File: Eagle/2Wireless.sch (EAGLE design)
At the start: 17 parts, among them IC1 TCA9517A, IC2 VREGLD1117, IC3 MB85RS2MTAPNF-G-BDERE1, U1 PHOTON_WITH_HEADERS

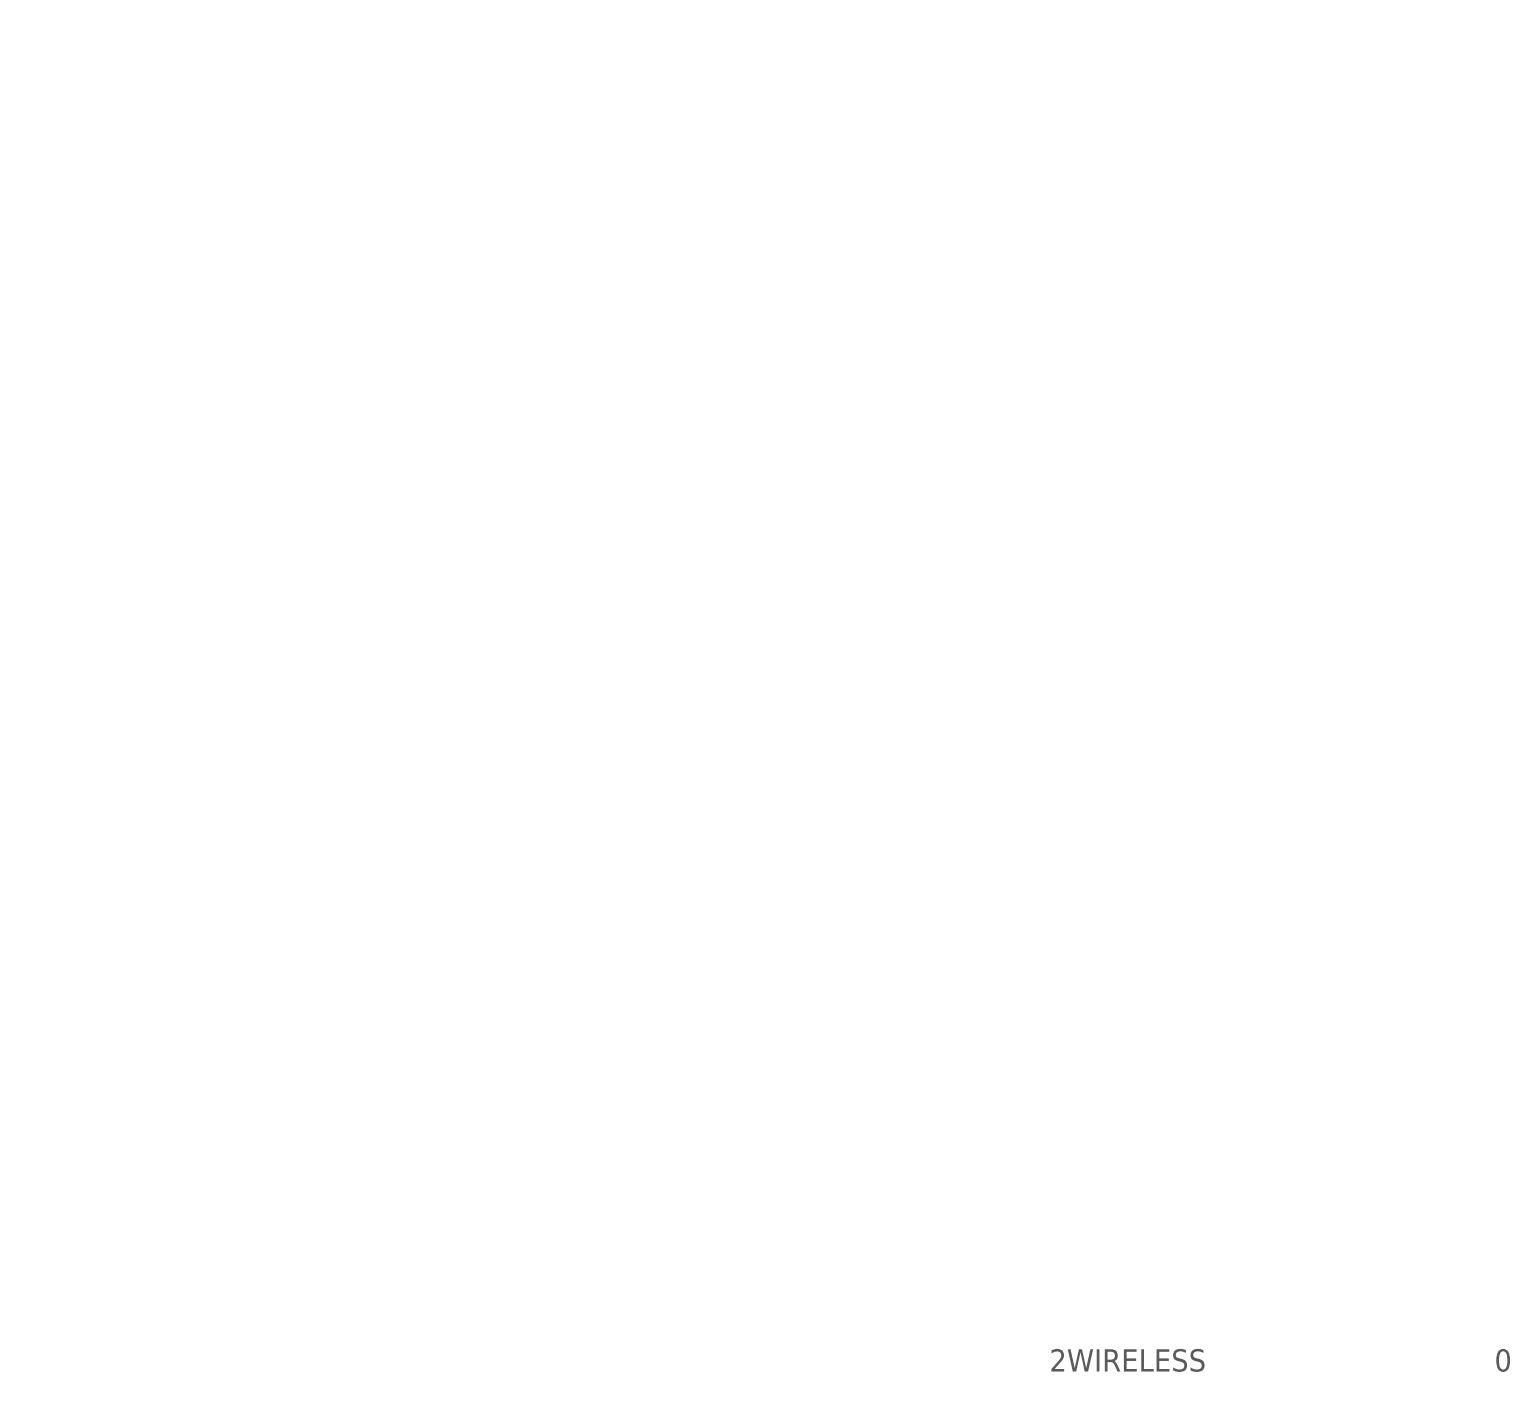
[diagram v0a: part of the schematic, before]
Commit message: Added two 24FC512. Photon unreliable as I2C slave.
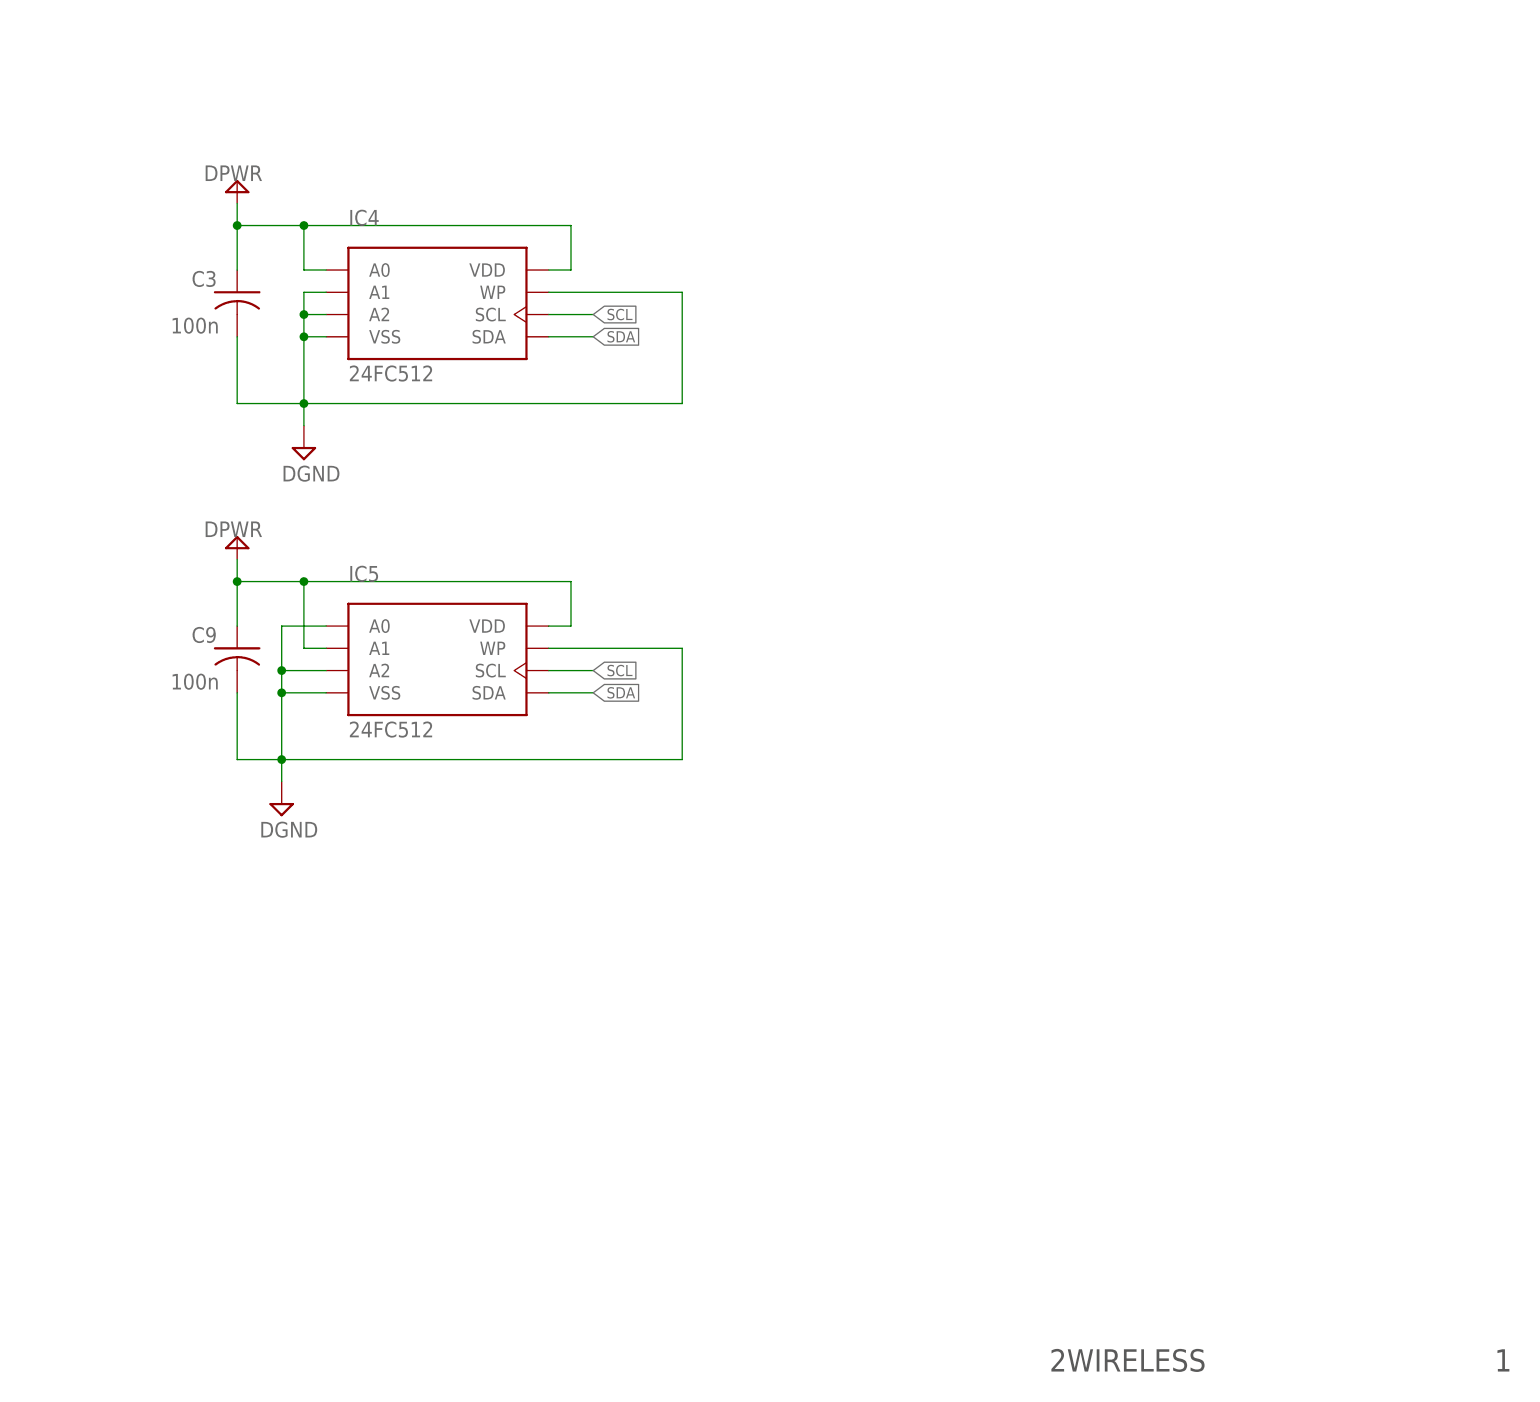
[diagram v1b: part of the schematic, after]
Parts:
- added C3, C9: 100n, studio_h:CB
- added IC4, IC5: 24FC512, studio_h:FRAM24FC512
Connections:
- net DGND: now also C3.2, C9.2, IC4.A1, IC4.A2, IC4.VSS, IC4.WP, IC5.A0, IC5.A2, IC5.VSS, IC5.WP
- net DPWR: now also C3.1, C9.1, IC4.A0, IC4.VDD, IC5.A1, IC5.VDD
- net SCL: now also IC4.SCL, IC5.SCL
- net SDA: now also IC4.SDA, IC5.SDA
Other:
- note added: "1"
- note removed: "0"
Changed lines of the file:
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@@
 <setting verticaltext="up"/>
 </settings>
-<grid distance="0.1" unitdist="inch" unit="inch" style="lines" multiple="1" display="no" altdistance="0.01" altunitdist="inch" altunit="inch"/>
+<grid distance="0.1" unitdist="inch" unit="inch" style="lines" multiple="1" display="yes" altdistance="0.01" altunitdist="inch" altunit="inch"/>
 <layers>
 <layer number="1" name="Top" color="4" fill="1" visible="no" active="no"/>
@@
 <part name="DPWR3" library="studio_h" deviceset="DPWR" device=""/>
 <part name="DPWR4" library="studio_h" deviceset="DPWR" device=""/>
+<part name="IC4" library="studio_h" deviceset="FRAM" device="24FC512" value="24FC512"/>
+<part name="DGND4" library="studio_h" deviceset="DGND" device=""/>
+<part name="DPWR5" library="studio_h" deviceset="DPWR" device=""/>
+<part name="C3" library="studio_h" deviceset="C" device="B" value="100n"/>
+<part name="IC5" library="studio_h" deviceset="FRAM" device="24FC512" value="24FC512"/>
+<part name="DGND3" library="studio_h" deviceset="DGND" device=""/>
+<part name="DPWR6" library="studio_h" deviceset="DPWR" device=""/>
+<part name="C9" library="studio_h" deviceset="C" device="B" value="100n"/>
 </parts>
 <sheets>
@@
 <plain>
 <text x="367.03" y="6.35" size="2.54" layer="97" font="vector" ratio="12">2WIRELESS</text>
-<text x="417.83" y="6.35" size="2.54" layer="97" font="vector" ratio="12">0</text>
+<text x="417.83" y="6.35" size="2.54" layer="97" font="vector" ratio="12">1</text>
 <text x="153.416" y="152.4" size="6.4516" layer="97" font="vector" ratio="12">3.3V Power</text>
 <text x="237.236" y="233.172" size="6.4516" layer="97" font="vector" ratio="12">Memory</text>
@@
 <instance part="DPWR3" gate="G$1" x="236.22" y="223.52"/>
 <instance part="DPWR4" gate="G$1" x="119.38" y="182.88"/>
+<instance part="IC4" gate="G$1" x="297.18" y="129.54"/>
+<instance part="DGND4" gate="G$1" x="281.94" y="111.76"/>
+<instance part="DPWR5" gate="G$1" x="274.32" y="139.7"/>
+<instance part="C3" gate="G$1" x="274.32" y="129.54" smashed="yes">
+<attribute name="NAME" x="272.034" y="131.953" size="1.778" layer="95" font="vector" ratio="12" rot="R180"/>
+<attribute name="VALUE" x="272.288" y="126.619" size="1.778" layer="96" font="vector" ratio="12" rot="R180"/>
+</instance>
+<instance part="IC5" gate="G$1" x="297.18" y="88.9"/>
+<instance part="DGND3" gate="G$1" x="279.4" y="71.12"/>
+<instance part="DPWR6" gate="G$1" x="274.32" y="99.06"/>
+<instance part="C9" gate="G$1" x="274.32" y="88.9" smashed="yes">
+<attribute name="NAME" x="272.034" y="91.313" size="1.778" layer="95" font="vector" ratio="12" rot="R180"/>
+<attribute name="VALUE" x="272.288" y="85.979" size="1.778" layer="96" font="vector" ratio="12" rot="R180"/>
+</instance>
 </instances>
 <busses>
@@
 <wire x1="86.36" y1="60.96" x2="68.58" y2="60.96" width="0.1524" layer="91"/>
 </segment>
+<segment>
+<pinref part="IC4" gate="G$1" pin="SCL"/>
+<wire x1="309.88" y1="127" x2="314.96" y2="127" width="0.1524" layer="91"/>
+<label x="314.96" y="127" size="1.27" layer="95" font="vector" ratio="12" xref="yes"/>
+</segment>
+<segment>
+<pinref part="IC5" gate="G$1" pin="SCL"/>
+<wire x1="309.88" y1="86.36" x2="314.96" y2="86.36" width="0.1524" layer="91"/>
+<label x="314.96" y="86.36" size="1.27" layer="95" font="vector" ratio="12" xref="yes"/>
+</segment>
 </net>
 <net name="SDA" class="0">
@@
 <pinref part="IC1" gate="G$1" pin="SDAB"/>
 <wire x1="86.36" y1="58.42" x2="76.2" y2="58.42" width="0.1524" layer="91"/>
+</segment>
+<segment>
+<pinref part="IC4" gate="G$1" pin="SDA"/>
+<wire x1="309.88" y1="124.46" x2="314.96" y2="124.46" width="0.1524" layer="91"/>
+<label x="314.96" y="124.46" size="1.27" layer="95" font="vector" ratio="12" xref="yes"/>
+</segment>
+<segment>
+<pinref part="IC5" gate="G$1" pin="SDA"/>
+<wire x1="309.88" y1="83.82" x2="314.96" y2="83.82" width="0.1524" layer="91"/>
+<label x="314.96" y="83.82" size="1.27" layer="95" font="vector" ratio="12" xref="yes"/>
 </segment>
 </net>
@@
 <wire x1="119.38" y1="55.88" x2="119.38" y2="53.34" width="0.1524" layer="91"/>
 </segment>
+<segment>
+<pinref part="IC4" gate="G$1" pin="VSS"/>
+<pinref part="DGND4" gate="G$1" pin="DGND"/>
+<wire x1="284.48" y1="124.46" x2="281.94" y2="124.46" width="0.1524" layer="91"/>
+<wire x1="281.94" y1="124.46" x2="281.94" y2="116.84" width="0.1524" layer="91"/>
+<pinref part="IC4" gate="G$1" pin="WP"/>
+<wire x1="281.94" y1="116.84" x2="281.94" y2="114.3" width="0.1524" layer="91"/>
+<wire x1="309.88" y1="129.54" x2="325.12" y2="129.54" width="0.1524" layer="91"/>
+<wire x1="325.12" y1="129.54" x2="325.12" y2="116.84" width="0.1524" layer="91"/>
+<wire x1="325.12" y1="116.84" x2="281.94" y2="116.84" width="0.1524" layer="91"/>
+<junction x="281.94" y="116.84"/>
+<pinref part="IC4" gate="G$1" pin="A2"/>
+<wire x1="284.48" y1="127" x2="281.94" y2="127" width="0.1524" layer="91"/>
+<wire x1="281.94" y1="127" x2="281.94" y2="124.46" width="0.1524" layer="91"/>
+<junction x="281.94" y="124.46"/>
+<pinref part="IC4" gate="G$1" pin="A1"/>
+<wire x1="284.48" y1="129.54" x2="281.94" y2="129.54" width="0.1524" layer="91"/>
+<wire x1="281.94" y1="129.54" x2="281.94" y2="127" width="0.1524" layer="91"/>
+<junction x="281.94" y="127"/>
+<pinref part="C3" gate="G$1" pin="2"/>
+<wire x1="281.94" y1="116.84" x2="274.32" y2="116.84" width="0.1524" layer="91"/>
+<wire x1="274.32" y1="116.84" x2="274.32" y2="124.46" width="0.1524" layer="91"/>
+</segment>
+<segment>
+<pinref part="IC5" gate="G$1" pin="VSS"/>
+<pinref part="DGND3" gate="G$1" pin="DGND"/>
+<wire x1="284.48" y1="83.82" x2="279.4" y2="83.82" width="0.1524" layer="91"/>
+<wire x1="279.4" y1="83.82" x2="279.4" y2="76.2" width="0.1524" layer="91"/>
+<pinref part="IC5" gate="G$1" pin="WP"/>
+<wire x1="279.4" y1="76.2" x2="279.4" y2="73.66" width="0.1524" layer="91"/>
+<wire x1="309.88" y1="88.9" x2="325.12" y2="88.9" width="0.1524" layer="91"/>
+<wire x1="325.12" y1="88.9" x2="325.12" y2="76.2" width="0.1524" layer="91"/>
+<wire x1="325.12" y1="76.2" x2="279.4" y2="76.2" width="0.1524" layer="91"/>
+<junction x="279.4" y="76.2"/>
+<pinref part="IC5" gate="G$1" pin="A2"/>
+<wire x1="284.48" y1="86.36" x2="279.4" y2="86.36" width="0.1524" layer="91"/>
+<wire x1="279.4" y1="86.36" x2="279.4" y2="83.82" width="0.1524" layer="91"/>
+<junction x="279.4" y="83.82"/>
+<pinref part="C9" gate="G$1" pin="2"/>
+<wire x1="279.4" y1="76.2" x2="274.32" y2="76.2" width="0.1524" layer="91"/>
+<wire x1="274.32" y1="76.2" x2="274.32" y2="83.82" width="0.1524" layer="91"/>
+<pinref part="IC5" gate="G$1" pin="A0"/>
+<wire x1="284.48" y1="91.44" x2="279.4" y2="91.44" width="0.1524" layer="91"/>
+<wire x1="279.4" y1="91.44" x2="279.4" y2="86.36" width="0.1524" layer="91"/>
+<junction x="279.4" y="86.36"/>
+</segment>
 </net>
 <net name="+5V" class="1">
@@
 <pinref part="DPWR4" gate="G$1" pin="DPWR"/>
 </segment>
-</net>
+<segment>
+<pinref part="IC4" gate="G$1" pin="VDD"/>
+<wire x1="309.88" y1="132.08" x2="312.42" y2="132.08" width="0.1524" layer="91"/>
+<wire x1="312.42" y1="132.08" x2="312.42" y2="137.16" width="0.1524" layer="91"/>
+<pinref part="DPWR5" gate="G$1" pin="DPWR"/>
+<wire x1="312.42" y1="137.16" x2="281.94" y2="137.16" width="0.1524" layer="91"/>
+<wire x1="281.94" y1="137.16" x2="274.32" y2="137.16" width="0.1524" layer="91"/>
+<wire x1="274.32" y1="137.16" x2="274.32" y2="139.7" width="0.1524" layer="91"/>
+<pinref part="C3" gate="G$1" pin="1"/>
+<wire x1="274.32" y1="132.08" x2="274.32" y2="137.16" width="0.1524" layer="91"/>
+<junction x="274.32" y="137.16"/>
+<pinref part="IC4" gate="G$1" pin="A0"/>
+<wire x1="284.48" y1="132.08" x2="281.94" y2="132.08" width="0.1524" layer="91"/>
+<wire x1="281.94" y1="132.08" x2="281.94" y2="137.16" width="0.1524" layer="91"/>
+<junction x="281.94" y="137.16"/>
+</segment>
+<segment>
+<pinref part="IC5" gate="G$1" pin="VDD"/>
+<wire x1="309.88" y1="91.44" x2="312.42" y2="91.44" width="0.1524" layer="91"/>
+<wire x1="312.42" y1="91.44" x2="312.42" y2="96.52" width="0.1524" layer="91"/>
+<pinref part="DPWR6" gate="G$1" pin="DPWR"/>
+<wire x1="312.42" y1="96.52" x2="281.94" y2="96.52" width="0.1524" layer="91"/>
+<wire x1="281.94" y1="96.52" x2="274.32" y2="96.52" width="0.1524" layer="91"/>
+<wire x1="274.32" y1="96.52" x2="274.32" y2="99.06" width="0.1524" layer="91"/>
+<pinref part="C9" gate="G$1" pin="1"/>
+<wire x1="274.32" y1="91.44" x2="274.32" y2="96.52" width="0.1524" layer="91"/>
+<junction x="274.32" y="96.52"/>
+<pinref part="IC5" gate="G$1" pin="A1"/>
+<wire x1="284.48" y1="88.9" x2="281.94" y2="88.9" width="0.1524" layer="91"/>
+<wire x1="281.94" y1="88.9" x2="281.94" y2="96.52" width="0.1524" layer="91"/>
+<junction x="281.94" y="96.52"/>
+</segment>
+</net>
